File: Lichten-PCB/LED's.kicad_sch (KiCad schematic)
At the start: 50 parts

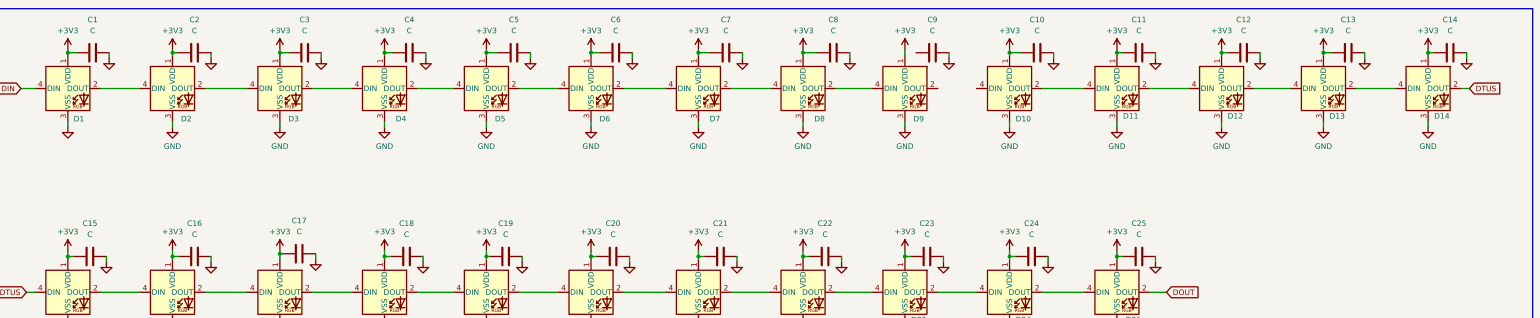
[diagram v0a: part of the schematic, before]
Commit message: Capacitor waardes toegevoegd en coonectoren toegevoegd
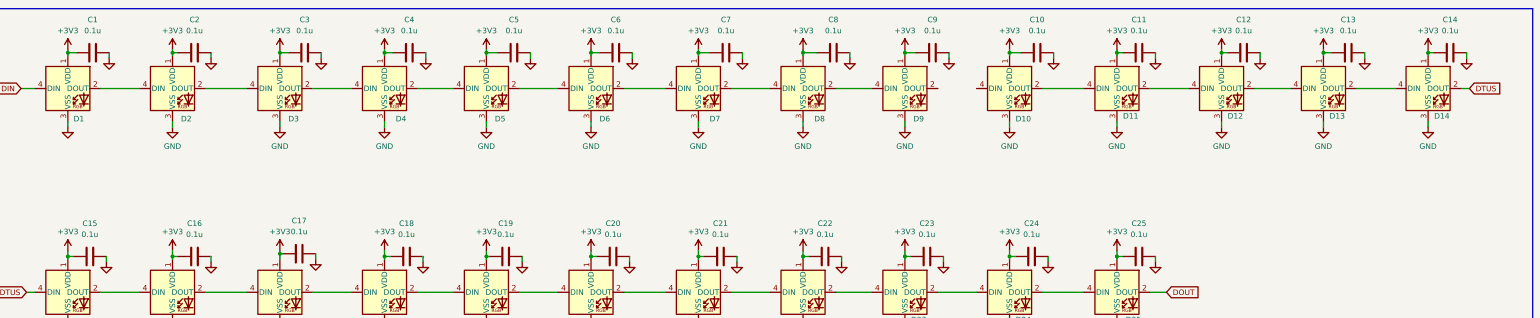
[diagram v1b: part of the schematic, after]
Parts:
- C1, C10, C11, C12, C13, C14, C15, C16, C17, C18, C19, C2, C20, C21, C22, C23, C24, C25, C3, C4, C5, C6, C7, C8, C9: value C -> 0.1u
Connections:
- net +3V3: now also C9.1
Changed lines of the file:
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@@
   (junction (at 214.63 96.52) (diameter 0) (color 0 0 0 0)
   )
+  (junction (at 238.125 49.53) (diameter 0) (color 0 0 0 0)
+  )
   (junction (at 118.11 49.53) (diameter 0) (color 0 0 0 0)
   )
@@
     (stroke (width 0) (type default))
   )
+  (wire (pts (xy 238.125 49.53) (xy 238.125 50.165))
+    (stroke (width 0) (type default))
+  )
   (wire (pts (xy 334.645 49.53) (xy 336.55 49.53))
     (stroke (width 0) (type default))
@@
     (stroke (width 0) (type default))
   )
-  (wire (pts (xy 238.125 48.895) (xy 238.125 50.165))
+  (wire (pts (xy 238.125 48.895) (xy 238.125 49.53))
     (stroke (width 0) (type default))
   )
@@
     (stroke (width 0) (type default))
   )
+  (wire (pts (xy 238.125 49.53) (xy 240.665 49.53))
+    (stroke (width 0) (type default))
+  )
   (wire (pts (xy 101.6 104.775) (xy 110.49 104.775))
     (stroke (width 0) (type default))
@@
       (effects (font (size 1.27 1.27)))
     )
-    (property "Value" "C" (at 196.85 44.45 90)
+    (property "Value" "0.1u" (at 196.85 44.45 90)
       (effects (font (size 1.27 1.27)))
     )
@@
       (effects (font (size 1.27 1.27)))
     )
-    (property "Value" "C" (at 243.205 91.44 90)
+    (property "Value" "0.1u" (at 243.205 91.44 90)
       (effects (font (size 1.27 1.27)))
     )
@@
       (effects (font (size 1.27 1.27)))
     )
-    (property "Value" "C" (at 267.335 91.44 90)
+    (property "Value" "0.1u" (at 267.335 91.44 90)
       (effects (font (size 1.27 1.27)))
     )
@@
       (effects (font (size 1.27 1.27)))
     )
-    (property "Value" "C" (at 195.58 91.44 90)
+    (property "Value" "0.1u" (at 195.58 91.44 90)
       (effects (font (size 1.27 1.27)))
     )
@@
       (effects (font (size 1.27 1.27)))
     )
-    (property "Value" "C" (at 98.425 90.805 90)
+    (property "Value" "0.1u" (at 98.425 90.805 90)
       (effects (font (size 1.27 1.27)))
     )
@@
       (effects (font (size 1.27 1.27)))
     )
-    (property "Value" "C" (at 292.1 44.45 90)
+    (property "Value" "0.1u" (at 292.1 44.45 90)
       (effects (font (size 1.27 1.27)))
     )
@@
       (effects (font (size 1.27 1.27)))
     )
-    (property "Value" "C" (at 171.45 44.45 90)
+    (property "Value" "0.1u" (at 171.45 44.45 90)
       (effects (font (size 1.27 1.27)))
     )
@@
       (effects (font (size 1.27 1.27)))
     )
-    (property "Value" "C" (at 123.19 91.44 90)
+    (property "Value" "0.1u" (at 123.19 91.44 90)
       (effects (font (size 1.27 1.27)))
     )
@@
       (effects (font (size 1.27 1.27)))
     )
-    (property "Value" "C" (at 363.855 44.45 90)
+    (property "Value" "0.1u" (at 363.855 44.45 90)
       (effects (font (size 1.27 1.27)))
     )
@@
       (effects (font (size 1.27 1.27)))
     )
-    (property "Value" "C" (at 170.815 91.44 90)
+    (property "Value" "0.1u" (at 170.815 91.44 90)
       (effects (font (size 1.27 1.27)))
     )
@@
       (effects (font (size 1.27 1.27)))
     )
-    (property "Value" "C" (at 99.695 44.45 90)
+    (property "Value" "0.1u" (at 99.695 44.45 90)
       (effects (font (size 1.27 1.27)))
     )
@@
       (effects (font (size 1.27 1.27)) hide)
     )
+    (property "Veld 4" "" (at 99.695 49.53 90)
+      (effects (font (size 1.27 1.27)) hide)
+    )
+    (property "Veld 5" "" (at 99.695 49.53 90)
+      (effects (font (size 1.27 1.27)) hide)
+    )
     (pin "1")
     (pin "2")
@@
       (effects (font (size 1.27 1.27)))
     )
-    (property "Value" "C" (at 147.955 44.45 90)
+    (property "Value" "0.1u" (at 147.955 44.45 90)
       (effects (font (size 1.27 1.27)))
     )
@@
       (effects (font (size 1.27 1.27)))
     )
-    (property "Value" "C" (at 50.165 91.44 90)
+    (property "Value" "0.1u" (at 50.165 91.44 90)
       (effects (font (size 1.27 1.27)))
     )
@@
       (effects (font (size 1.27 1.27)))
     )
-    (property "Value" "C" (at 219.71 91.44 90)
+    (property "Value" "0.1u" (at 219.71 91.44 90)
       (effects (font (size 1.27 1.27)))
     )
@@
       (effects (font (size 1.27 1.27)))
     )
-    (property "Value" "C" (at 316.23 44.45 90)
+    (property "Value" "0.1u" (at 316.23 44.45 90)
       (effects (font (size 1.27 1.27)))
     )
@@
       (effects (font (size 1.27 1.27)))
     )
-    (property "Value" "C" (at 268.605 44.45 90)
+    (property "Value" "0.1u" (at 268.605 44.45 90)
       (effects (font (size 1.27 1.27)))
     )
@@
       (effects (font (size 1.27 1.27)))
     )
-    (property "Value" "C" (at 340.36 44.45 90)
+    (property "Value" "0.1u" (at 340.36 44.45 90)
       (effects (font (size 1.27 1.27)))
     )
@@
       (effects (font (size 1.27 1.27)))
     )
-    (property "Value" "C" (at 244.475 44.45 90)
+    (property "Value" "0.1u" (at 244.475 44.45 90)
       (effects (font (size 1.27 1.27)))
     )
@@
       (effects (font (size 1.27 1.27)))
     )
-    (property "Value" "C" (at 74.295 91.44 90)
+    (property "Value" "0.1u" (at 74.295 91.44 90)
       (effects (font (size 1.27 1.27)))
     )
@@
       (effects (font (size 1.27 1.27)))
     )
-    (property "Value" "C" (at 50.8 44.45 90)
+    (property "Value" "0.1u" (at 50.8 44.45 90)
       (effects (font (size 1.27 1.27)))
     )
@@
       (effects (font (size 1.27 1.27)))
     )
-    (property "Value" "C" (at 123.825 44.45 90)
+    (property "Value" "0.1u" (at 123.825 44.45 90)
       (effects (font (size 1.27 1.27)))
     )
@@
       (effects (font (size 1.27 1.27)))
     )
-    (property "Value" "C" (at 146.05 91.44 90)
+    (property "Value" "0.1u" (at 146.05 91.44 90)
       (effects (font (size 1.27 1.27)))
     )
@@
       (effects (font (size 1.27 1.27)))
     )
-    (property "Value" "C" (at 221.615 44.45 90)
+    (property "Value" "0.1u" (at 221.615 44.45 90)
       (effects (font (size 1.27 1.27)))
     )
@@
       (effects (font (size 1.27 1.27)))
     )
-    (property "Value" "C" (at 292.1 91.44 90)
+    (property "Value" "0.1u" (at 292.1 91.44 90)
       (effects (font (size 1.27 1.27)))
     )
@@
       (effects (font (size 1.27 1.27)))
     )
-    (property "Value" "C" (at 74.295 44.45 90)
+    (property "Value" "0.1u" (at 74.295 44.45 90)
       (effects (font (size 1.27 1.27)))
     )

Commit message: Footprints toegevoegd
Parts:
- C1, C10, C11, C12, C13, C14, C15, C16, C17, C18, C19, C2, C20, C21, C22, C23, C24, C25, C3, C4, C5, C6, C7, C8, C9: footprint (none) -> Capacitor_SMD:C_0603_1608Metric
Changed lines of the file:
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@@
       (effects (font (size 1.27 1.27)))
     )
-    (property "Footprint" "" (at 200.66 48.5648 0)
+    (property "Footprint" "Capacitor_SMD:C_0603_1608Metric" (at 200.66 48.5648 0)
       (effects (font (size 1.27 1.27)) hide)
     )
@@
       (effects (font (size 1.27 1.27)))
     )
-    (property "Footprint" "" (at 247.015 95.5548 0)
+    (property "Footprint" "Capacitor_SMD:C_0603_1608Metric" (at 247.015 95.5548 0)
       (effects (font (size 1.27 1.27)) hide)
     )
@@
       (effects (font (size 1.27 1.27)))
     )
-    (property "Footprint" "" (at 271.145 95.5548 0)
+    (property "Footprint" "Capacitor_SMD:C_0603_1608Metric" (at 271.145 95.5548 0)
       (effects (font (size 1.27 1.27)) hide)
     )
@@
       (effects (font (size 1.27 1.27)))
     )
-    (property "Footprint" "" (at 199.39 95.5548 0)
+    (property "Footprint" "Capacitor_SMD:C_0603_1608Metric" (at 199.39 95.5548 0)
       (effects (font (size 1.27 1.27)) hide)
     )
@@
       (effects (font (size 1.27 1.27)))
     )
-    (property "Footprint" "" (at 102.235 94.9198 0)
+    (property "Footprint" "Capacitor_SMD:C_0603_1608Metric" (at 102.235 94.9198 0)
       (effects (font (size 1.27 1.27)) hide)
     )
@@
       (effects (font (size 1.27 1.27)))
     )
-    (property "Footprint" "" (at 295.91 48.5648 0)
+    (property "Footprint" "Capacitor_SMD:C_0603_1608Metric" (at 295.91 48.5648 0)
       (effects (font (size 1.27 1.27)) hide)
     )
@@
       (effects (font (size 1.27 1.27)))
     )
-    (property "Footprint" "" (at 175.26 48.5648 0)
+    (property "Footprint" "Capacitor_SMD:C_0603_1608Metric" (at 175.26 48.5648 0)
       (effects (font (size 1.27 1.27)) hide)
     )
@@
       (effects (font (size 1.27 1.27)))
     )
-    (property "Footprint" "" (at 127 95.5548 0)
+    (property "Footprint" "Capacitor_SMD:C_0603_1608Metric" (at 127 95.5548 0)
       (effects (font (size 1.27 1.27)) hide)
     )
@@
       (effects (font (size 1.27 1.27)))
     )
-    (property "Footprint" "" (at 367.665 48.5648 0)
+    (property "Footprint" "Capacitor_SMD:C_0603_1608Metric" (at 367.665 48.5648 0)
       (effects (font (size 1.27 1.27)) hide)
     )
@@
       (effects (font (size 1.27 1.27)))
     )
-    (property "Footprint" "" (at 174.625 95.5548 0)
+    (property "Footprint" "Capacitor_SMD:C_0603_1608Metric" (at 174.625 95.5548 0)
       (effects (font (size 1.27 1.27)) hide)
     )
@@
       (effects (font (size 1.27 1.27)))
     )
-    (property "Footprint" "" (at 103.505 48.5648 0)
+    (property "Footprint" "Capacitor_SMD:C_0603_1608Metric" (at 103.505 48.5648 0)
       (effects (font (size 1.27 1.27)) hide)
     )
@@
       (effects (font (size 1.27 1.27)))
     )
-    (property "Footprint" "" (at 151.765 48.5648 0)
+    (property "Footprint" "Capacitor_SMD:C_0603_1608Metric" (at 151.765 48.5648 0)
       (effects (font (size 1.27 1.27)) hide)
     )
@@
       (effects (font (size 1.27 1.27)))
     )
-    (property "Footprint" "" (at 53.975 95.5548 0)
+    (property "Footprint" "Capacitor_SMD:C_0603_1608Metric" (at 53.975 95.5548 0)
       (effects (font (size 1.27 1.27)) hide)
     )
@@
       (effects (font (size 1.27 1.27)))
     )
-    (property "Footprint" "" (at 223.52 95.5548 0)
+    (property "Footprint" "Capacitor_SMD:C_0603_1608Metric" (at 223.52 95.5548 0)
       (effects (font (size 1.27 1.27)) hide)
     )
@@
       (effects (font (size 1.27 1.27)))
     )
-    (property "Footprint" "" (at 320.04 48.5648 0)
+    (property "Footprint" "Capacitor_SMD:C_0603_1608Metric" (at 320.04 48.5648 0)
       (effects (font (size 1.27 1.27)) hide)
     )
@@
       (effects (font (size 1.27 1.27)))
     )
-    (property "Footprint" "" (at 272.415 48.5648 0)
+    (property "Footprint" "Capacitor_SMD:C_0603_1608Metric" (at 272.415 48.5648 0)
       (effects (font (size 1.27 1.27)) hide)
     )
@@
       (effects (font (size 1.27 1.27)))
     )
-    (property "Footprint" "" (at 344.17 48.5648 0)
+    (property "Footprint" "Capacitor_SMD:C_0603_1608Metric" (at 344.17 48.5648 0)
       (effects (font (size 1.27 1.27)) hide)
     )
@@
       (effects (font (size 1.27 1.27)))
     )
-    (property "Footprint" "" (at 248.285 48.5648 0)
+    (property "Footprint" "Capacitor_SMD:C_0603_1608Metric" (at 248.285 48.5648 0)
       (effects (font (size 1.27 1.27)) hide)
     )
@@
       (effects (font (size 1.27 1.27)))
     )
-    (property "Footprint" "" (at 78.105 95.5548 0)
+    (property "Footprint" "Capacitor_SMD:C_0603_1608Metric" (at 78.105 95.5548 0)
       (effects (font (size 1.27 1.27)) hide)
     )
@@
       (effects (font (size 1.27 1.27)))
     )
-    (property "Footprint" "" (at 54.61 48.5648 0)
+    (property "Footprint" "Capacitor_SMD:C_0603_1608Metric" (at 54.61 48.5648 0)
       (effects (font (size 1.27 1.27)) hide)
     )
@@
       (effects (font (size 1.27 1.27)))
     )
-    (property "Footprint" "" (at 127.635 48.5648 0)
+    (property "Footprint" "Capacitor_SMD:C_0603_1608Metric" (at 127.635 48.5648 0)
       (effects (font (size 1.27 1.27)) hide)
     )
@@
       (effects (font (size 1.27 1.27)))
     )
-    (property "Footprint" "" (at 149.86 95.5548 0)
+    (property "Footprint" "Capacitor_SMD:C_0603_1608Metric" (at 149.86 95.5548 0)
       (effects (font (size 1.27 1.27)) hide)
     )
@@
       (effects (font (size 1.27 1.27)))
     )
-    (property "Footprint" "" (at 225.425 48.5648 0)
+    (property "Footprint" "Capacitor_SMD:C_0603_1608Metric" (at 225.425 48.5648 0)
       (effects (font (size 1.27 1.27)) hide)
     )
@@
       (effects (font (size 1.27 1.27)))
     )
-    (property "Footprint" "" (at 295.91 95.5548 0)
+    (property "Footprint" "Capacitor_SMD:C_0603_1608Metric" (at 295.91 95.5548 0)
       (effects (font (size 1.27 1.27)) hide)
     )
@@
       (effects (font (size 1.27 1.27)))
     )
-    (property "Footprint" "" (at 78.105 48.5648 0)
-      (effects (font (size 1.27 1.27)) hide)
-    )
+    (property "Footprint" "Capacitor_SMD:C_0603_1608Metric" (at 78.105 48.5648 0)
+      (effects (font (size 1.27 1.27)) hide)
+    )

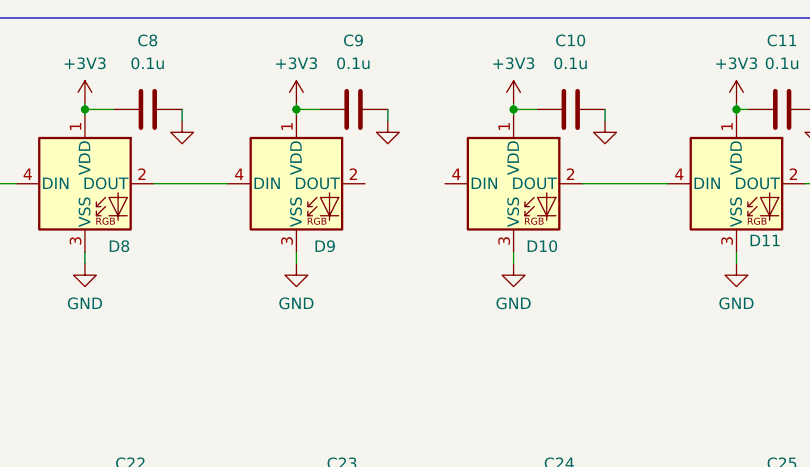
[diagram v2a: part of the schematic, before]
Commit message: Componenten geplaatst
Paar fouten opgelost namen juist gemaakt en niet gelinked connecties vastgemaakt.
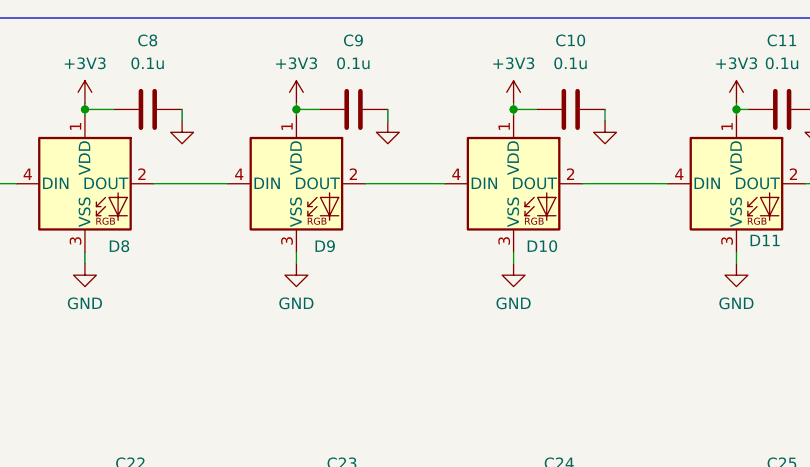
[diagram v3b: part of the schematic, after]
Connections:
- net at D10.4 (DIN): now also D9.2 (DOUT)
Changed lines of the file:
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@@
+    (stroke (width 0) (type default))
+  )
+  (wire (pts (xy 245.745 57.785) (xy 254.635 57.785))
     (stroke (width 0) (type default))
   )

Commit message: Edge cuts en via toegevoegd met wat silk screen
Misschien op de achterkant een leuke foto van een aap
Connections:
- net Data-6: now reaches D6.2 (DOUT), D7.4 (DIN)
- net Data-5: now reaches D5.2 (DOUT), D6.4 (DIN)
- net Data-22: now reaches D22.2 (DOUT), D23.4 (DIN)
- net Data-21: now reaches D21.2 (DOUT), D22.4 (DIN)
- net Data-17: now reaches D17.2 (DOUT), D18.4 (DIN)
- net Data-16: now reaches D16.2 (DOUT), D17.4 (DIN)
- net Data-3: now reaches D3.2 (DOUT), D4.4 (DIN)
- net Data-2: now reaches D2.2 (DOUT), D3.4 (DIN)
- net Data-13: now reaches D13.2 (DOUT), D14.4 (DIN)
- net Data-12: now reaches D12.2 (DOUT), D13.4 (DIN)
- net Data-15: now reaches D15.2 (DOUT), D16.4 (DIN)
- net Data-20: now reaches D20.2 (DOUT), D21.4 (DIN)
- net Data-18: now reaches D18.2 (DOUT), D19.4 (DIN)
- net Data-4: now reaches D4.2 (DOUT), D5.4 (DIN)
- net Data-11: now reaches D11.2 (DOUT), D12.4 (DIN)
- net Data-19: now reaches D19.2 (DOUT), D20.4 (DIN)
- net Data-1: now reaches D1.2 (DOUT), D2.4 (DIN)
- net Data-23: now reaches D23.2 (DOUT), D24.4 (DIN)
- net Data-24: now reaches D24.2 (DOUT), D25.4 (DIN)
- net Data-7: now reaches D7.2 (DOUT), D8.4 (DIN)
- net Data-10: now reaches D10.2 (DOUT), D11.4 (DIN)
- net Data-8: now reaches D8.2 (DOUT), D9.4 (DIN)
- net Data-9: now reaches D10.4 (DIN), D9.2 (DOUT)
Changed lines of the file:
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@@
+    (effects (font (size 1.27 1.27)) (justify left bottom))
+  )
+  (label "Data-5" (at 149.225 57.785 0) (fields_autoplaced)
+    (effects (font (size 1.27 1.27)) (justify left bottom))
+  )
+  (label "Data-2" (at 78.105 57.785 0) (fields_autoplaced)
+    (effects (font (size 1.27 1.27)) (justify left bottom))
+  )
+  (label "Data-9" (at 247.015 57.785 0) (fields_autoplaced)
+    (effects (font (size 1.27 1.27)) (justify left bottom))
+  )
+  (label "Data-11" (at 295.275 57.785 0) (fields_autoplaced)
+    (effects (font (size 1.27 1.27)) (justify left bottom))
+  )
+  (label "Data-23" (at 246.38 104.775 0) (fields_autoplaced)
+    (effects (font (size 1.27 1.27)) (justify left bottom))
+  )
+  (label "Data-16" (at 76.835 104.775 0) (fields_autoplaced)
+    (effects (font (size 1.27 1.27)) (justify left bottom))
+  )
+  (label "Data-21" (at 198.755 104.775 0) (fields_autoplaced)
+    (effects (font (size 1.27 1.27)) (justify left bottom))
+  )
+  (label "Data-13" (at 342.9 57.785 0) (fields_autoplaced)
+    (effects (font (size 1.27 1.27)) (justify left bottom))
+  )
+  (label "Data-6" (at 173.99 57.785 0) (fields_autoplaced)
+    (effects (font (size 1.27 1.27)) (justify left bottom))
+  )
+  (label "Data-8" (at 222.885 57.785 0) (fields_autoplaced)
+    (effects (font (size 1.27 1.27)) (justify left bottom))
+  )
+  (label "Data-1" (at 53.975 57.785 0) (fields_autoplaced)
+    (effects (font (size 1.27 1.27)) (justify left bottom))
+  )
+  (label "Data-10" (at 270.51 57.785 0) (fields_autoplaced)
+    (effects (font (size 1.27 1.27)) (justify left bottom))
+  )
+  (label "Data-19" (at 149.225 104.775 0) (fields_autoplaced)
+    (effects (font (size 1.27 1.27)) (justify left bottom))
+  )
+  (label "Data-12" (at 318.77 57.785 0) (fields_autoplaced)
+    (effects (font (size 1.27 1.27)) (justify left bottom))
+  )
+  (label "Data-17" (at 101.6 104.775 0) (fields_autoplaced)
+    (effects (font (size 1.27 1.27)) (justify left bottom))
+  )
+  (label "Data-24" (at 270.51 104.775 0) (fields_autoplaced)
+    (effects (font (size 1.27 1.27)) (justify left bottom))
+  )
+  (label "Data-18" (at 126.365 104.775 0) (fields_autoplaced)
+    (effects (font (size 1.27 1.27)) (justify left bottom))
+  )
+  (label "Data-22" (at 222.885 104.775 0) (fields_autoplaced)
+    (effects (font (size 1.27 1.27)) (justify left bottom))
+  )
+  (label "Data-3" (at 104.14 57.785 0) (fields_autoplaced)
+    (effects (font (size 1.27 1.27)) (justify left bottom))
+  )
+  (label "Data-15" (at 52.705 104.775 0) (fields_autoplaced)
+    (effects (font (size 1.27 1.27)) (justify left bottom))
+  )
+  (label "Data-7" (at 198.755 57.785 0) (fields_autoplaced)
+    (effects (font (size 1.27 1.27)) (justify left bottom))
+  )
+  (label "Data-20" (at 173.99 104.775 0) (fields_autoplaced)
+    (effects (font (size 1.27 1.27)) (justify left bottom))
+  )
+  (label "Data-4" (at 126.365 57.785 0) (fields_autoplaced)
     (effects (font (size 1.27 1.27)) (justify left bottom))
   )

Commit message: PCB vergroot
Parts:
- added C26, C27, C28, C29, C30, C31, C32, C33, C34, C35: 0.1u, Capacitor_SMD:C_0603_1608Metric, symbol Device:C
- added D26, D27, D28, D29, D30, D31, D32, D33, D34, D35: WS2812B, LED_SMD:LED_WS2812B_PLCC4_5.0x5.0mm_P3.2mm, symbol LED:WS2812B
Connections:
- net +3V3: now also C26.1, C27.1, C28.1, C29.1, C30.1, C31.1, C32.1, C33.1, C34.1, C35.1, D26.1 (VDD), D27.1 (VDD), D28.1 (VDD), D29.1 (VDD), D30.1 (VDD), D31.1 (VDD), D32.1 (VDD), D33.1 (VDD), D34.1 (VDD), D35.1 (VDD)
- net DOUT: now also D35.2 (DOUT); no longer D25.2 (DOUT)
- net GND: now also C26.2, C27.2, C28.2, C29.2, C30.2, C31.2, C32.2, C33.2, C34.2, C35.2, D26.3 (VSS), D27.3 (VSS), D28.3 (VSS), D29.3 (VSS), D30.3 (VSS), D31.3 (VSS), D32.3 (VSS), D33.3 (VSS), D34.3 (VSS), D35.3 (VSS)
- net DTUS renamed DTUS1
- new net DTUS2: D25.2 (DOUT), D26.4 (DIN)
- new net Data-25: D26.2 (DOUT), D27.4 (DIN)
- new net Data-26: D27.2 (DOUT), D28.4 (DIN)
- new net Data-27: D28.2 (DOUT), D29.4 (DIN)
- new net Data-28: D29.2 (DOUT), D30.4 (DIN)
- new net Data-29: D30.2 (DOUT), D31.4 (DIN)
- new net Data-30: D31.2 (DOUT), D32.4 (DIN)
- new net Data-31: D32.2 (DOUT), D33.4 (DIN)
- new net Data-32: D33.2 (DOUT), D34.4 (DIN)
- new net Data-33: D34.2 (DOUT), D35.4 (DIN)
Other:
- moved on the sheet: C25, D25
